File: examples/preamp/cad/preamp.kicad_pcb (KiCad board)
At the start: 2 copper layers, 68 parts, among them CON1 AVR-ISP-10, J1 Conn_01x04, J10 Conn_01x04, J11 CONN_01X03, J12 Conn_01x03, J13 Conn_01x03, J14 Conn_01x03, J15 CONN_01X03, J16 CONN_01X03, J17 CONN_01X03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

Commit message: Update preamp pcb
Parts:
- added REF**: MountingHole_3.2mm_M3, MountingHole:MountingHole_3.2mm_M3, F.Cu at (241.3, 26.7)
- added REF**: MountingHole_3.2mm_M3, MountingHole:MountingHole_3.2mm_M3, F.Cu at (241.3, 114.3)
- added REF**: MountingHole_3.2mm_M3, MountingHole:MountingHole_3.2mm_M3, F.Cu at (41.9, 114.3)
- added REF**: MountingHole_3.2mm_M3, MountingHole:MountingHole_3.2mm_M3, F.Cu at (41.9, 26.7)
- moved J6 77.3 mm to (108.0, 52.1)
- moved R6 46.6 mm to (96.5, 58.4), turned to 0 degrees
- moved R8 42.6 mm to (64.8, 77.5)
- moved C23 35.6 mm to (238.8, 63.5)
- moved R1 33.2 mm to (67.3, 40.6)
- moved J17 31.4 mm to (153.7, 82.5)
- moved J14 31.1 mm to (214.6, 102.9)
- moved J5 31.0 mm to (106.7, 68.6), turned to 180 degrees
- moved Q1 30.9 mm to (59.7, 77.5), turned to 180 degrees
- moved J8 30.7 mm to (62.2, 69.8), turned to 0 degrees
- moved C16 30.5 mm to (186.7, 49.5), turned to 90 degrees
- moved J9 29.9 mm to (55.9, 91.4), turned to 270 degrees
- moved J11 29.9 mm to (53.3, 61.0), turned to 180 degrees
- moved C10 29.5 mm to (214.6, 91.4)
- moved C2 29.3 mm to (78.7, 28.1), turned to 270 degrees
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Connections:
- J2 pad 1: Net-(J2-Pad1) -> GND
- J3 pad 1: Net-(J2-Pad1) -> GND
- J4 pad 1: Net-(J2-Pad1) -> GND
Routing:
- net GND: track 0.00 -> 447.6 mm
- net GNDA: track 0.00 -> 383.4 mm, vias 0 -> 2
- net VCC: track 0.00 -> 319.7 mm, vias 0 -> 8
- net /PowerBTN_MISO: track 0.00 -> 158.4 mm, vias 0 -> 5
- net /SCL: track 0.00 -> 144.1 mm
- net /SDA: track 0.00 -> 140.6 mm, vias 0 -> 2
- net /+9V: track 0.00 -> 91.9 mm
- net /RIGHT: track 0.00 -> 79.5 mm, vias 0 -> 2
- net /LEFT: track 0.00 -> 77.0 mm, vias 0 -> 2
- net /BTN3_MOSI: track 0.00 -> 72.1 mm, vias 0 -> 2
- net /Reset: track 0.00 -> 63.9 mm, vias 0 -> 2
- net /Input2Btn: track 0.00 -> 58.5 mm, vias 0 -> 2
- net /BTN1: track 0.00 -> 48.1 mm
- net /BTN0: track 0.00 -> 47.9 mm, vias 0 -> 2
- net /Input3Btn: track 0.00 -> 46.9 mm, vias 0 -> 2
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- added copper zone on B.Cu, net GND
- added copper zone on B.Cu, net GNDA
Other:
- board outline added: 209.6 x 97.8 mm

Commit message: Preamp PCB update
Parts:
- moved J17 20.5 mm to (156.2, 102.9), turned to 0 degrees
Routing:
- net /RIGHT: track 79.5 -> 102.3 mm
- net Net-(C10-Pad1): track 9.22 -> 30.5 mm, vias 1 -> 2
- net /LEFT: track 77.0 -> 97.7 mm
- net /BTN2: track 44.9 -> 49.5 mm
- net GNDA: track 383.4 -> 387.2 mm
- net Net-(J5-Pad3): track 8.42 -> 10.7 mm
- net VCC: track 319.7 -> 318.2 mm
- net /Input1BTN_SCK: track 31.5 -> 32.9 mm
- net /Input3Btn: track 46.9 -> 48.0 mm
- net /BTN3_MOSI: track 72.1 -> 73.0 mm
- removed copper zone on B.Cu, net GND
- removed copper zone on B.Cu, net GNDA
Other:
- board text added: "+5VOut"
- board text added: "+PowerIn"
- board text added: "CancelBtn"
- board text added: "DownBtn"
- board text added: "Encoder"
- board text added: "IR Reciever"
- board text added: "Input1"
- board text added: "Input1Btn"
- board text added: "Input2"
- board text added: "Input2Btn"
- board text added: "Input3"
- board text added: "Input3Btn"
- board text added: "LCD"
- board text added: "Output"
- board text added: "Power&Relay"
- board text added: "PowerBtn"
- board text added: "UpBtn"

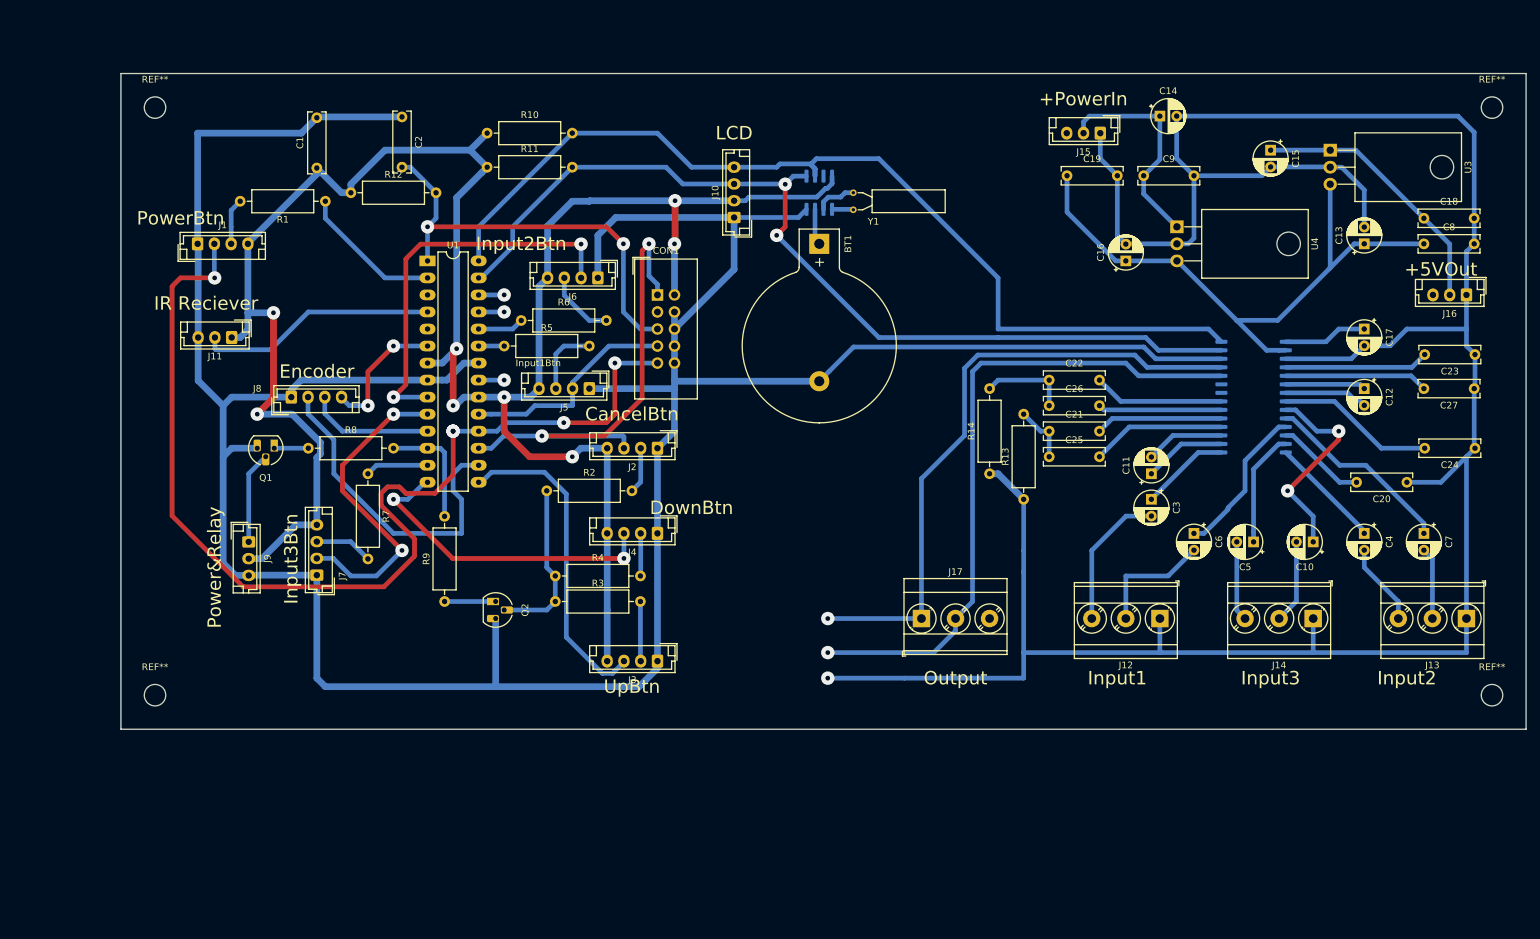
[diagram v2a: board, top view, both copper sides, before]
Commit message: Preamp PCB update
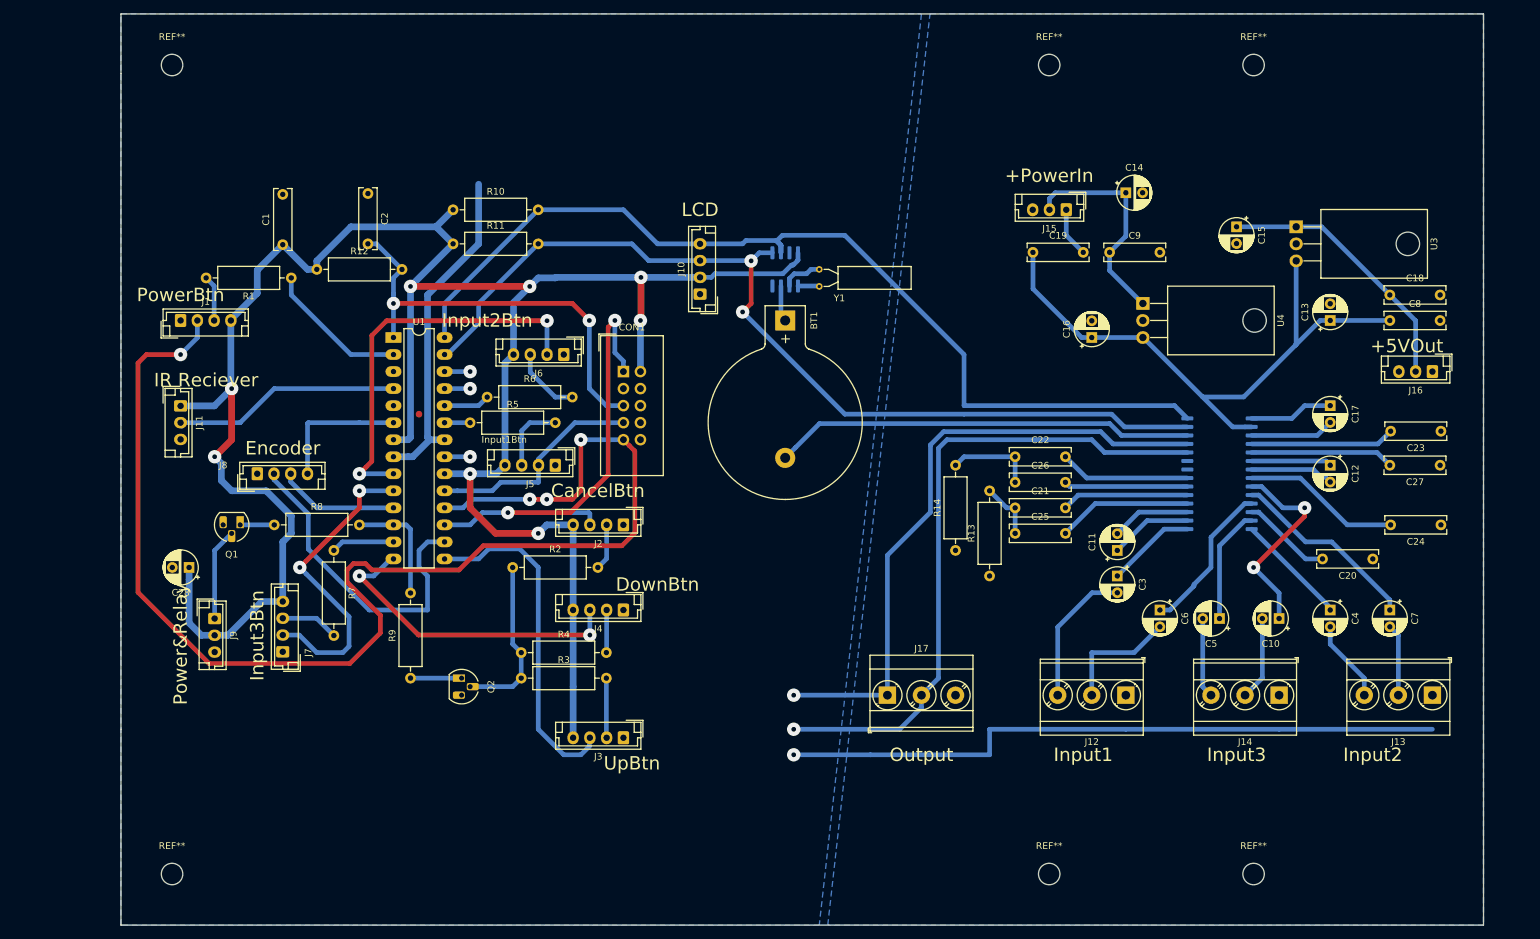
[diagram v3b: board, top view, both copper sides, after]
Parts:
- added C28: 100uF, Capacitor_THT:CP_Radial_D5.0mm_P2.50mm, F.Cu at (47.0, 95.2)
- added REF**: MountingHole_3.2mm_M3, MountingHole:MountingHole_3.2mm_M3, F.Cu at (205.7, 141.0)
- added REF**: MountingHole_3.2mm_M3, MountingHole:MountingHole_3.2mm_M3, F.Cu at (205.7, 20.3)
- moved REF** 71.2 mm to (175.3, 141.0)
- moved REF** 66.3 mm to (175.3, 20.3)
- moved REF** 26.8 mm to (44.5, 141.0)
- moved J11 12.7 mm to (45.7, 71.2), turned to 270 degrees
- moved C12 12.5 mm to (217.2, 80.0)
- moved C17 12.5 mm to (217.2, 71.1)
- moved C5 12.5 mm to (200.7, 102.9)
- moved J16 12.5 mm to (232.4, 66.0)
- moved J5 12.5 mm to (101.6, 80.0)
- moved U5 12.5 mm to (200.7, 81.3)
- moved Y1 12.5 mm to (141.0, 53.3)
- moved J9 12.5 mm to (50.8, 102.9)
- moved CON1 12.5 mm to (111.8, 66.0)
- moved J2 12.5 mm to (111.8, 88.9)
- moved J3 12.5 mm to (111.8, 120.7)
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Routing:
- net GND: track 447.6 -> 113.1 mm
- net GNDA: track 387.2 -> 123.2 mm
- net /PowerBTN_MISO: track 158.4 -> 199.6 mm, vias 5 -> 4
- net VCC: track 318.2 -> 335.3 mm
- net /BTN1: track 48.1 -> 50.9 mm
- net /IRint: track 35.8 -> 34.1 mm
- net /Input3Btn: track 48.0 -> 46.7 mm
- net /BTN2: track 49.5 -> 48.6 mm
- net /ENC1: track 18.9 -> 18.1 mm
- net /ENC0: track 20.1 -> 20.4 mm, vias 2 -> 0
- added copper zone on B.Cu, net GND
- added copper zone on B.Cu, net GNDA
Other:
- board size 209.6 x 97.8 mm -> 203.2 x 135.9 mm

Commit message: preamp: fix R value
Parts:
- R9: value 10k -> 47k
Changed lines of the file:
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@@
-(kicad_pcb (version 20171130) (host pcbnew 5.1.4+dfsg1-1)
+(kicad_pcb (version 20171130) (host pcbnew 5.1.5+dfsg1-2build2)
   (general
     (thickness 1.6)
@@
       (effects (font (size 1 1) (thickness 0.15)))
     )
-    (fp_text value 10k (at 6.35 2.72 90) (layer F.Fab)
+    (fp_text value 47k (at 6.35 2.72 90) (layer F.Fab)
       (effects (font (size 1 1) (thickness 0.15)))
     )
